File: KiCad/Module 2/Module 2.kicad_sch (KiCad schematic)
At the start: 15 parts

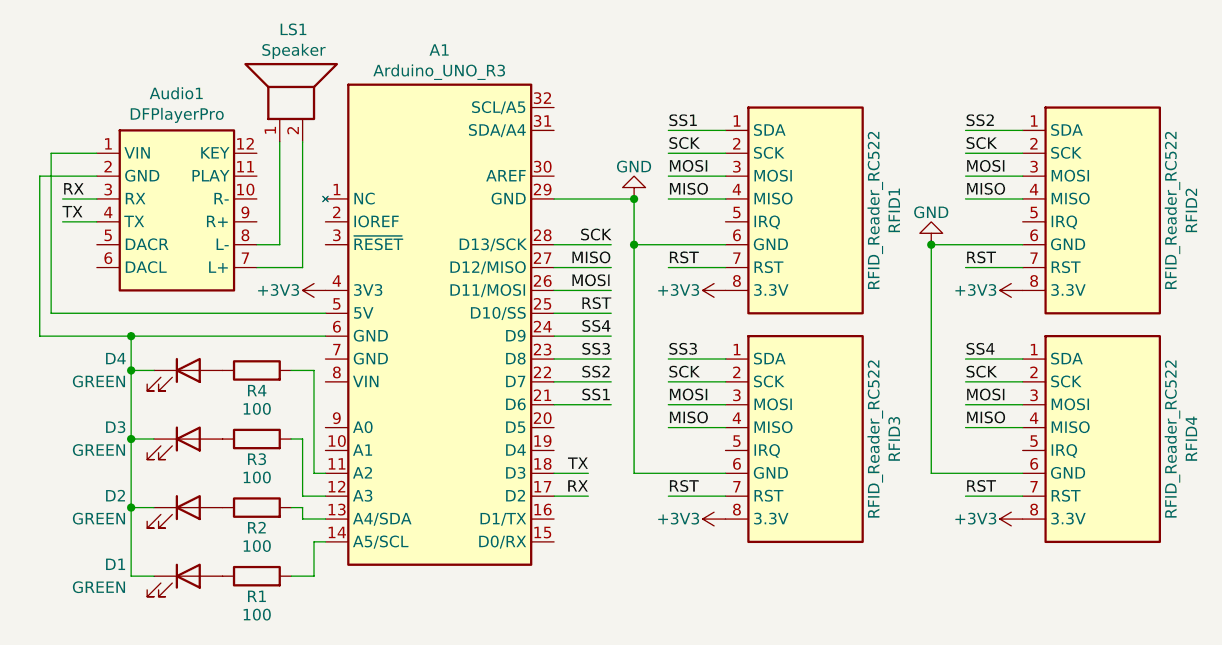
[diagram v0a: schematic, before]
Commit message: M2 - Updated Schematic
Added ESP32 to the Module 2 schematic.
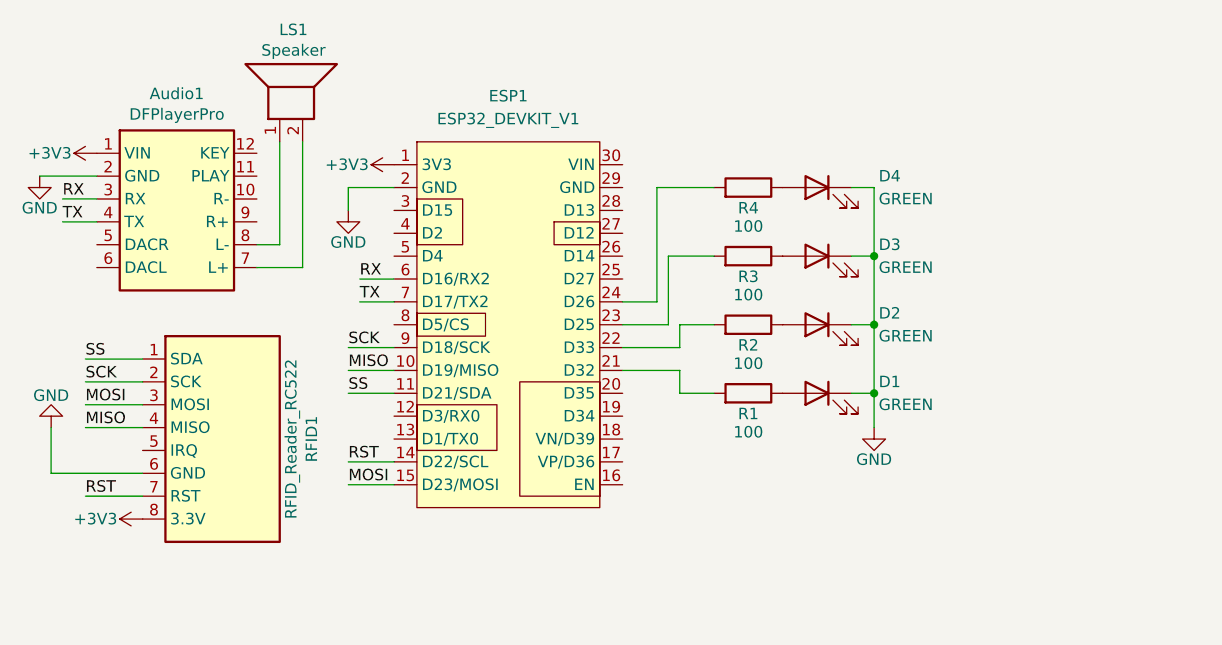
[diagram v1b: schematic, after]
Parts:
- removed A1: Arduino_UNO_R3, symbol IEEE_CS_Escape_Room_Symbols_v1:Arduino_UNO_R3
- removed RFID2, RFID3, RFID4: RFID_Reader_RC522, symbol IEEE_CS_Escape_Room_Symbols_v1:RFID_Reader_RC522
- added ESP1: ESP32_DEVKIT_V1, symbol IEEE_CS_Escape_Room_Symbols_v2:ESP32_DEVKIT_V1
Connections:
- net +3V3: now also Audio1.1 (VIN), ESP1.1 (3V3)
- net GND: now also Audio1.2 (GND), D1.1 (K), D2.1 (K), D3.1 (K), D4.1 (K), ESP1.2 (GND)
- net MISO: now also ESP1.10 (D19/MISO)
- net MOSI: now also ESP1.15 (D23/MOSI)
- net RST: now also ESP1.14 (D22/SCL)
- net RX: now also ESP1.6 (D16/RX2)
- net SCK: now also ESP1.9 (D18/SCK)
- net TX: now also ESP1.7 (D17/TX2)
- net at R1.2: now also ESP1.21 (D32)
- net at R2.2: now also ESP1.22 (D33)
- net at R4.2: now also ESP1.24 (D26)
- net at R3.2: now also ESP1.23 (D25)
- net SS1 renamed SS
- net SS: now also ESP1.11 (D21/SDA)
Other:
- moved on the sheet: D1, D2, D3, D4, R1, R2, R3, R4, RFID1
